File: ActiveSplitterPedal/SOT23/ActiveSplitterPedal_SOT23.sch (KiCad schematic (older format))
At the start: 18 parts, among them J1 MonoJack2Switch, J2 MonoJack2Switch, J3 MonoJack2Switch, J4 MonoJack2Switch, J5 MonoJack2Switch, J6 Barrel_Jack, SW1 SW_DIP_x04

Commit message: updated schematic
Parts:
- removed SW1: SW_DIP_x04, Button_Switch_SMD:SW_DIP_SPSTx04_Slide_6.7x11.72mm_W6.73mm_P2.54mm_LowProfile_JPin, symbol Switch:SW_DIP_x04
- added SW1, SW2, SW3, SW4: SW_SPST, Connector_PinHeader_2.54mm:PinHeader_1x02_P2.54mm_Vertical, symbol Switch:SW_SPST
- D1, D2, D3, D4: footprint LED_SMD:LED_0805_2012Metric_Pad1.15x1.40mm_HandSolder -> LED_THT:LED_D5.0mm
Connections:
- net +5V: now also SW1.1 (A), SW2.1 (A), SW3.1 (A), SW4.1 (A)
- net BUFFER_SW1: now also R1.2, SW1.2 (B); no longer R4.2
- net BUFFER_SW2: now also R2.2, SW2.2 (B); no longer R3.2
- net BUFFER_SW3: now also R3.2, SW3.2 (B); no longer R2.2
- net BUFFER_SW4: now also R4.2, SW4.2 (B); no longer R1.2
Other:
- moved on the sheet: D1, D2, D3, D4, J6, R1, R2, R3, R4

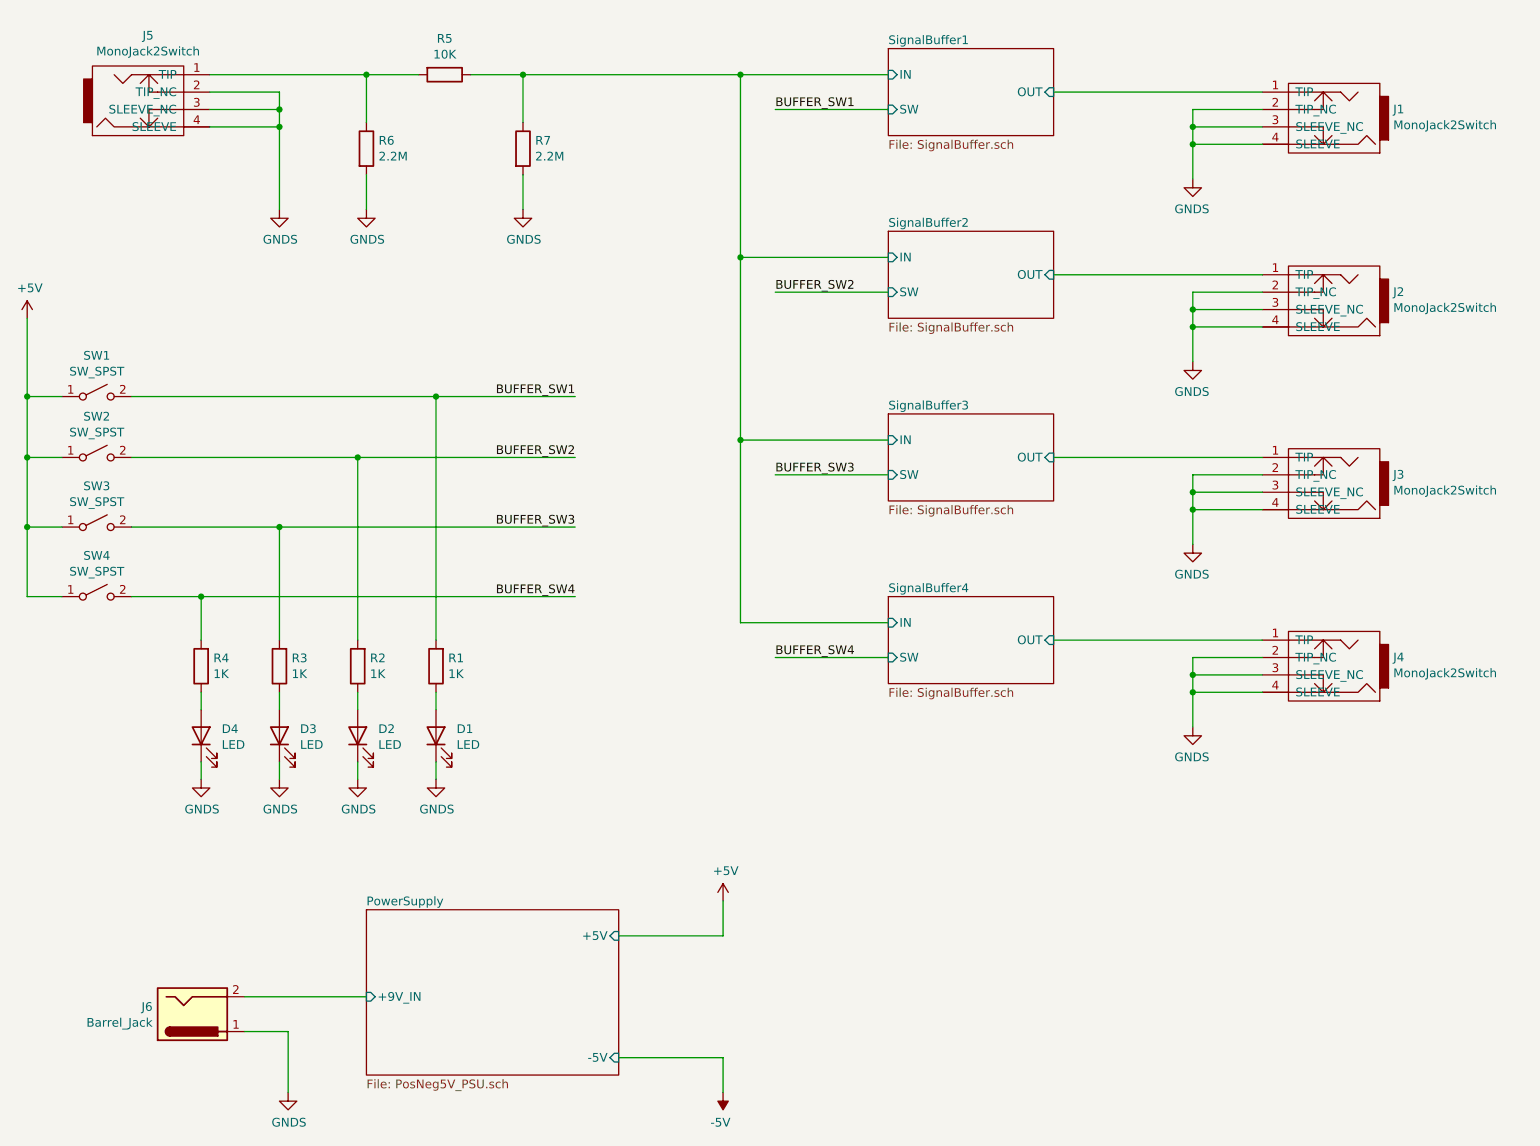
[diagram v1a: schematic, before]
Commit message: SOT23 REVA draft layout completed
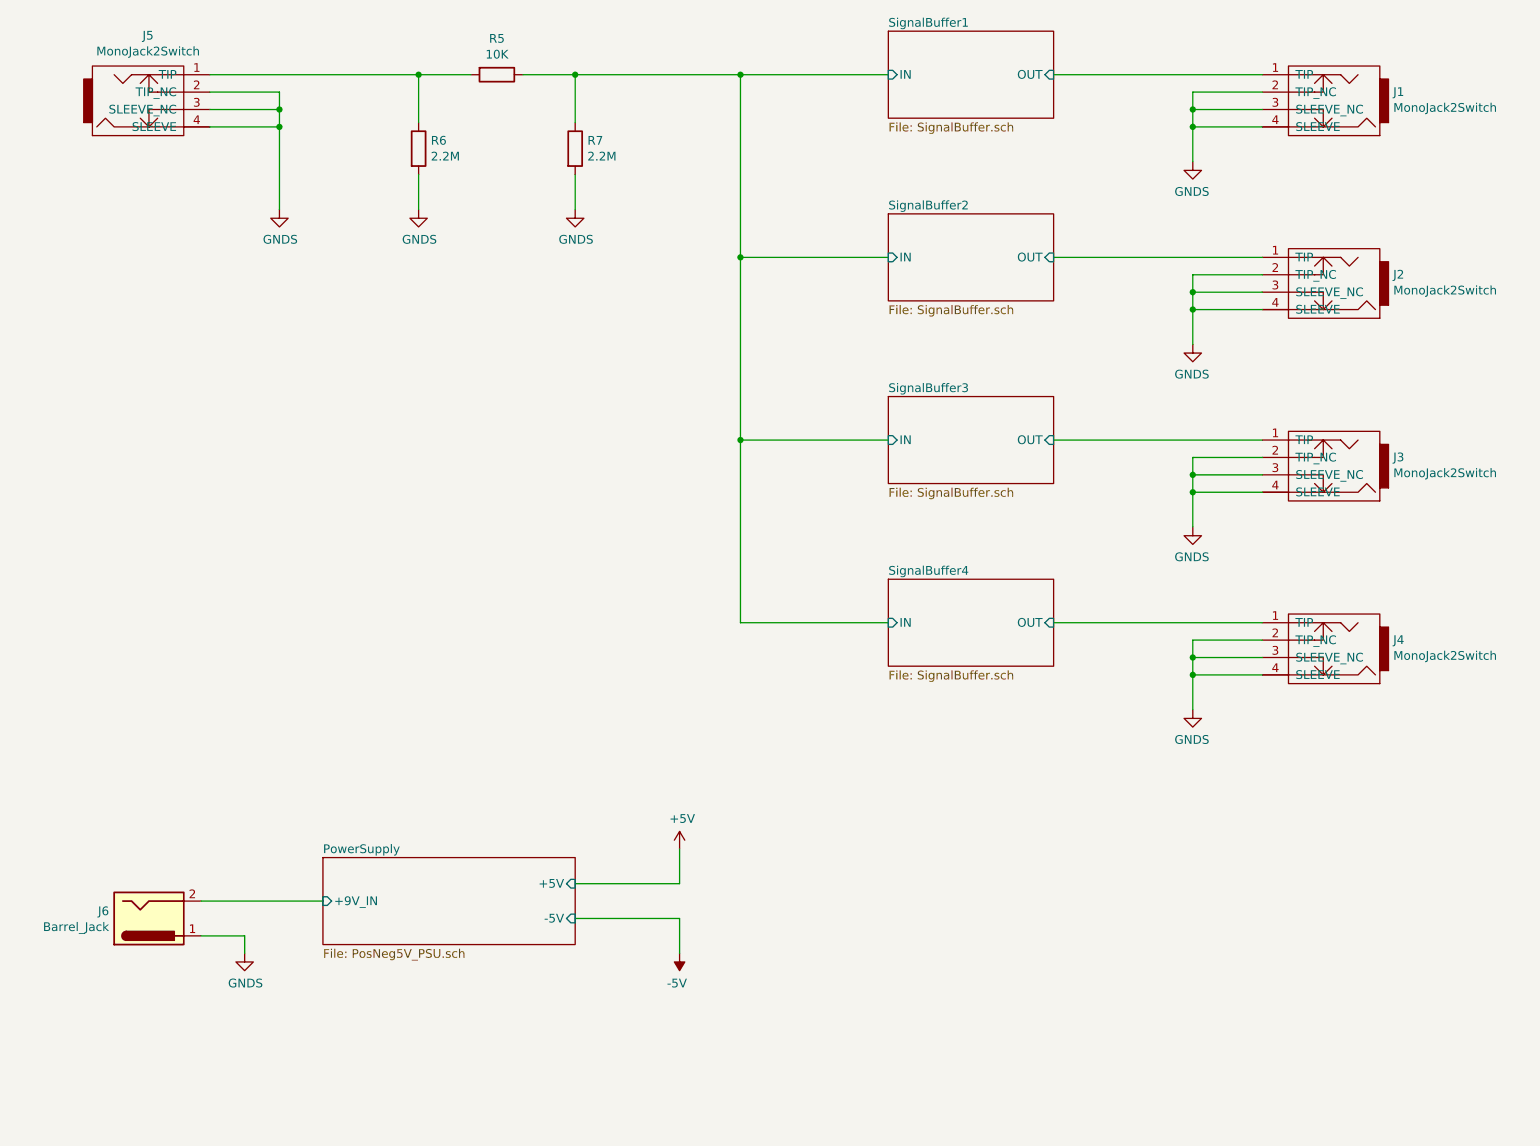
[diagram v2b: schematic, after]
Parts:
- removed D1, D2, D3, D4: LED, LED_THT:LED_D5.0mm, symbol Device:LED
- removed R1, R2, R3, R4: 1K, Resistor_SMD:R_0805_2012Metric_Pad1.15x1.40mm_HandSolder, symbol Device:R
- removed SW1, SW2, SW3, SW4: SW_SPST, Connector_PinHeader_2.54mm:PinHeader_1x02_P2.54mm_Vertical, symbol Switch:SW_SPST
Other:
- moved on the sheet: J1, J2, J3, J4, J6, R5, R6, R7

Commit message: Completed RevA layout
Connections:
- net SignalBuffer1/IN renamed GainAndPeakDetector1/SIGNAL_INPUT
- net SignalBuffer1/OUT renamed GainAndPeakDetector1/SIGNAL_OUTPUT
- net SignalBuffer2/OUT renamed GainAndPeakDetector2/SIGNAL_OUTPUT
- net SignalBuffer3/OUT renamed GainAndPeakDetector3/SIGNAL_OUTPUT
- net SignalBuffer4/OUT renamed GainAndPeakDetector4/SIGNAL_OUTPUT
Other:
- moved on the sheet: J1, J2, J3, J4
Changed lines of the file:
@@
 L MonoJack2Switch:MonoJack2Switch J1
 U 1 1 5F366B64
-P 8950 1450
-F 0 "J1" H 8648 1501 50  0000 R CNN
-F 1 "MonoJack2Switch" H 8648 1410 50  0000 R CNN
-F 2 "NeutrikNRJ:NRJxHx" H 8950 1500 50  0001 C CNN
-F 3 "https://www.neutrik.com/en/product/nrj6hm-1-pre" H 8950 1500 50  0001 C CNN
-	1    8950 1450
+P 8950 1600
+F 0 "J1" H 8648 1651 50  0000 R CNN
+F 1 "MonoJack2Switch" H 8648 1560 50  0000 R CNN
+F 2 "NeutrikNRJ:NRJxHx" H 8950 1650 50  0001 C CNN
+F 3 "https://www.neutrik.com/en/product/nrj6hm-1-pre" H 8950 1650 50  0001 C CNN
+	1    8950 1600
 	-1   0    0    -1
 $EndComp
@@
 L MonoJack2Switch:MonoJack2Switch J2
 U 1 1 5F369E69
-P 8950 2500
-F 0 "J2" H 8648 2551 50  0000 R CNN
-F 1 "MonoJack2Switch" H 8648 2460 50  0000 R CNN
-F 2 "NeutrikNRJ:NRJxHx" H 8950 2550 50  0001 C CNN
-F 3 "https://www.neutrik.com/en/product/nrj6hm-1-pre" H 8950 2550 50  0001 C CNN
-	1    8950 2500
+P 8950 2650
+F 0 "J2" H 8648 2701 50  0000 R CNN
+F 1 "MonoJack2Switch" H 8648 2610 50  0000 R CNN
+F 2 "NeutrikNRJ:NRJxHx" H 8950 2700 50  0001 C CNN
+F 3 "https://www.neutrik.com/en/product/nrj6hm-1-pre" H 8950 2700 50  0001 C CNN
+	1    8950 2650
 	-1   0    0    -1
 $EndComp
@@
 L MonoJack2Switch:MonoJack2Switch J3
 U 1 1 5F36BD50
-P 8950 3550
-F 0 "J3" H 8648 3601 50  0000 R CNN
-F 1 "MonoJack2Switch" H 8648 3510 50  0000 R CNN
-F 2 "NeutrikNRJ:NRJxHx" H 8950 3600 50  0001 C CNN
-F 3 "https://www.neutrik.com/en/product/nrj6hm-1-pre" H 8950 3600 50  0001 C CNN
-	1    8950 3550
+P 8950 3700
+F 0 "J3" H 8648 3751 50  0000 R CNN
+F 1 "MonoJack2Switch" H 8648 3660 50  0000 R CNN
+F 2 "NeutrikNRJ:NRJxHx" H 8950 3750 50  0001 C CNN
+F 3 "https://www.neutrik.com/en/product/nrj6hm-1-pre" H 8950 3750 50  0001 C CNN
+	1    8950 3700
 	-1   0    0    -1
 $EndComp
@@
 L MonoJack2Switch:MonoJack2Switch J4
 U 1 1 5F36CF2A
-P 8950 4600
-F 0 "J4" H 8648 4651 50  0000 R CNN
-F 1 "MonoJack2Switch" H 8648 4560 50  0000 R CNN
-F 2 "NeutrikNRJ:NRJxHx" H 8950 4650 50  0001 C CNN
-F 3 "https://www.neutrik.com/en/product/nrj6hm-1-pre" H 8950 4650 50  0001 C CNN
-	1    8950 4600
+P 8950 4750
+F 0 "J4" H 8648 4801 50  0000 R CNN
+F 1 "MonoJack2Switch" H 8648 4710 50  0000 R CNN
+F 2 "NeutrikNRJ:NRJxHx" H 8950 4800 50  0001 C CNN
+F 3 "https://www.neutrik.com/en/product/nrj6hm-1-pre" H 8950 4800 50  0001 C CNN
+	1    8950 4750
 	-1   0    0    -1
 $EndComp
@@
 $EndComp
 Wire Wire Line
-	8500 1400 8100 1400
-Wire Wire Line
-	8100 1400 8100 1500
-Wire Wire Line
-	8500 1500 8100 1500
-Connection ~ 8100 1500
-Wire Wire Line
-	8100 1500 8100 1600
-Wire Wire Line
-	8500 1600 8100 1600
-Connection ~ 8100 1600
-Wire Wire Line
-	8100 1600 8100 1800
+	8500 1550 8100 1550
+Wire Wire Line
+	8100 1550 8100 1650
+Wire Wire Line
+	8500 1650 8100 1650
+Connection ~ 8100 1650
+Wire Wire Line
+	8100 1650 8100 1750
+Wire Wire Line
+	8500 1750 8100 1750
+Connection ~ 8100 1750
+Wire Wire Line
+	8100 1750 8100 1950
 $Comp
 L power:GNDS #PWR012
 U 1 1 5F3AA43F
-P 8100 1800
-F 0 "#PWR012" H 8100 1550 50  0001 C CNN
-F 1 "GNDS" H 8105 1627 50  0000 C CNN
-F 2 "" H 8100 1800 50  0001 C CNN
-F 3 "" H 8100 1800 50  0001 C CNN
-	1    8100 1800
-	-1   0    0    -1
-$EndComp
-Wire Wire Line
-	8500 2450 8100 2450
-Wire Wire Line
-	8100 2450 8100 2550
-Wire Wire Line
-	8500 2550 8100 2550
-Connection ~ 8100 2550
-Wire Wire Line
-	8100 2550 8100 2650
-Wire Wire Line
-	8500 2650 8100 2650
-Connection ~ 8100 2650
-Wire Wire Line
-	8100 2650 8100 2850
+P 8100 1950
+F 0 "#PWR012" H 8100 1700 50  0001 C CNN
+F 1 "GNDS" H 8105 1777 50  0000 C CNN
+F 2 "" H 8100 1950 50  0001 C CNN
+F 3 "" H 8100 1950 50  0001 C CNN
+	1    8100 1950
+	-1   0    0    -1
+$EndComp
+Wire Wire Line
+	8500 2600 8100 2600
+Wire Wire Line
+	8100 2600 8100 2700
+Wire Wire Line
+	8500 2700 8100 2700
+Connection ~ 8100 2700
+Wire Wire Line
+	8100 2700 8100 2800
+Wire Wire Line
+	8500 2800 8100 2800
+Connection ~ 8100 2800
+Wire Wire Line
+	8100 2800 8100 3000
 $Comp
 L power:GNDS #PWR013
 U 1 1 5F3ABE1D
-P 8100 2850
-F 0 "#PWR013" H 8100 2600 50  0001 C CNN
-F 1 "GNDS" H 8105 2677 50  0000 C CNN
-F 2 "" H 8100 2850 50  0001 C CNN
-F 3 "" H 8100 2850 50  0001 C CNN
-	1    8100 2850
-	-1   0    0    -1
-$EndComp
-Wire Wire Line
-	8500 3500 8100 3500
-Wire Wire Line
-	8100 3500 8100 3600
-Wire Wire Line
-	8500 3600 8100 3600
-Connection ~ 8100 3600
-Wire Wire Line
-	8100 3600 8100 3700
-Wire Wire Line
-	8500 3700 8100 3700
-Connection ~ 8100 3700
-Wire Wire Line
-	8100 3700 8100 3900
+P 8100 3000
+F 0 "#PWR013" H 8100 2750 50  0001 C CNN
+F 1 "GNDS" H 8105 2827 50  0000 C CNN
+F 2 "" H 8100 3000 50  0001 C CNN
+F 3 "" H 8100 3000 50  0001 C CNN
+	1    8100 3000
+	-1   0    0    -1
+$EndComp
+Wire Wire Line
+	8500 3650 8100 3650
+Wire Wire Line
+	8100 3650 8100 3750
+Wire Wire Line
+	8500 3750 8100 3750
+Connection ~ 8100 3750
+Wire Wire Line
+	8100 3750 8100 3850
+Wire Wire Line
+	8500 3850 8100 3850
+Connection ~ 8100 3850
+Wire Wire Line
+	8100 3850 8100 4050
 $Comp
 L power:GNDS #PWR014
 U 1 1 5F3ADB89
-P 8100 3900
-F 0 "#PWR014" H 8100 3650 50  0001 C CNN
-F 1 "GNDS" H 8105 3727 50  0000 C CNN
-F 2 "" H 8100 3900 50  0001 C CNN
-F 3 "" H 8100 3900 50  0001 C CNN
-	1    8100 3900
-	-1   0    0    -1
-$EndComp
-Wire Wire Line
-	8500 4550 8100 4550
-Wire Wire Line
-	8100 4550 8100 4650
-Wire Wire Line
-	8500 4650 8100 4650
-Connection ~ 8100 4650
-Wire Wire Line
-	8100 4650 8100 4750
-Wire Wire Line
-	8500 4750 8100 4750
-Connection ~ 8100 4750
-Wire Wire Line
-	8100 4750 8100 4950
+P 8100 4050
+F 0 "#PWR014" H 8100 3800 50  0001 C CNN
+F 1 "GNDS" H 8105 3877 50  0000 C CNN
+F 2 "" H 8100 4050 50  0001 C CNN
+F 3 "" H 8100 4050 50  0001 C CNN
+	1    8100 4050
+	-1   0    0    -1
+$EndComp
+Wire Wire Line
+	8500 4700 8100 4700
+Wire Wire Line
+	8100 4700 8100 4800
+Wire Wire Line
+	8500 4800 8100 4800
+Connection ~ 8100 4800
+Wire Wire Line
+	8100 4800 8100 4900
+Wire Wire Line
+	8500 4900 8100 4900
+Connection ~ 8100 4900
+Wire Wire Line
+	8100 4900 8100 5100
 $Comp
 L power:GNDS #PWR015
 U 1 1 5F3AF94C
-P 8100 4950
-F 0 "#PWR015" H 8100 4700 50  0001 C CNN
-F 1 "GNDS" H 8105 4777 50  0000 C CNN
-F 2 "" H 8100 4950 50  0001 C CNN
-F 3 "" H 8100 4950 50  0001 C CNN
-	1    8100 4950
+P 8100 5100
+F 0 "#PWR015" H 8100 4850 50  0001 C CNN
+F 1 "GNDS" H 8105 4927 50  0000 C CNN
+F 2 "" H 8100 5100 50  0001 C CNN
+F 3 "" H 8100 5100 50  0001 C CNN
+	1    8100 5100
 	-1   0    0    -1
 $EndComp
@@
 $EndSheet
 Wire Wire Line
-	7300 2350 8500 2350
-Wire Wire Line
-	7300 3400 8500 3400
-Wire Wire Line
-	7300 4450 8500 4450
-Wire Wire Line
-	7300 1300 8500 1300
+	7150 2500 8500 2500
+Wire Wire Line
+	7150 3550 8500 3550
+Wire Wire Line
+	7150 4600 8500 4600
+Wire Wire Line
+	7150 1450 8500 1450
 Wire Wire Line
 	4550 1300 5500 1300
@@
 	5500 4450 6350 4450
 $Sheet
-S 6350 4200 950  500
-U 5F365B82
-F0 "SignalBuffer4" 50
-F1 "SignalBuffer.sch" 50
-F2 "IN" I L 6350 4450 50
-F3 "OUT" I R 7300 4450 50
-$EndSheet
-$Sheet
-S 6350 3150 950  500
-U 5F365961
-F0 "SignalBuffer3" 50
-F1 "SignalBuffer.sch" 50
-F2 "IN" I L 6350 3400 50
-F3 "OUT" I R 7300 3400 50
-$EndSheet
-$Sheet
-S 6350 2100 950  500
-U 5F3658F9
-F0 "SignalBuffer2" 50
-F1 "SignalBuffer.sch" 50
-F2 "IN" I L 6350 2350 50
-F3 "OUT" I R 7300 2350 50
-$EndSheet
-$Sheet
-S 6350 1050 950  500
-U 5F350192
-F0 "SignalBuffer1" 50
-F1 "SignalBuffer.sch" 50
-F2 "IN" I L 6350 1300 50
-F3 "OUT" I R 7300 1300 50
+S 6350 2200 800  450
+U 5F512144
+F0 "GainAndPeakDetector2" 50
+F1 "InvGainAndPeakDetector.sch" 50
+F2 "SIGNAL_INPUT" I L 6350 2350 50
+F3 "SIGNAL_OUTPUT" I R 7150 2500 50
+$EndSheet
+$Sheet
+S 6350 3250 800  450
+U 5F515E89
+F0 "GainAndPeakDetector3" 50
+F1 "InvGainAndPeakDetector.sch" 50
+F2 "SIGNAL_INPUT" I L 6350 3400 50
+F3 "SIGNAL_OUTPUT" I R 7150 3550 50
+$EndSheet
+$Sheet
+S 6350 4300 800  450
+U 5F519B24
+F0 "GainAndPeakDetector4" 50
+F1 "InvGainAndPeakDetector.sch" 50
+F2 "SIGNAL_INPUT" I L 6350 4450 50
+F3 "SIGNAL_OUTPUT" I R 7150 4600 50
+$EndSheet
+$Sheet
+S 6350 1150 800  450
+U 5F3F1F31
+F0 "GainAndPeakDetector1" 50
+F1 "InvGainAndPeakDetector.sch" 50
+F2 "SIGNAL_INPUT" I L 6350 1300 50
+F3 "SIGNAL_OUTPUT" I R 7150 1450 50
 $EndSheet
 $EndSCHEMATC
